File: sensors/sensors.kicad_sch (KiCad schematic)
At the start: 3 parts, among them J1 GPIO, J2 PWM, J3 Conn_01x16

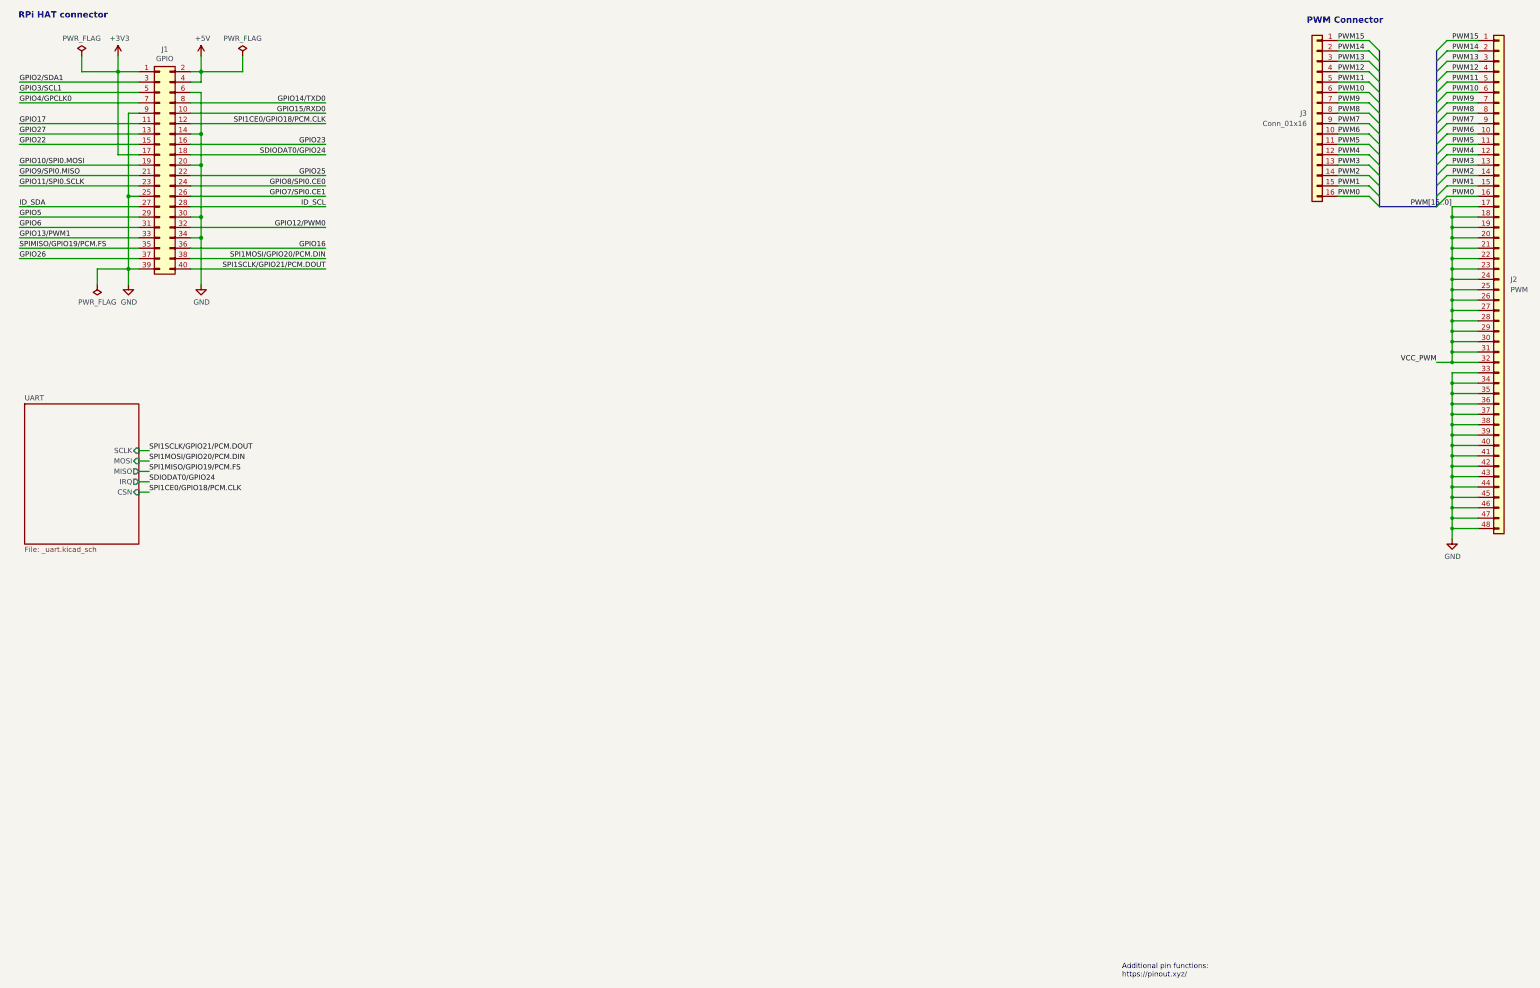
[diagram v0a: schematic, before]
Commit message: add IMU
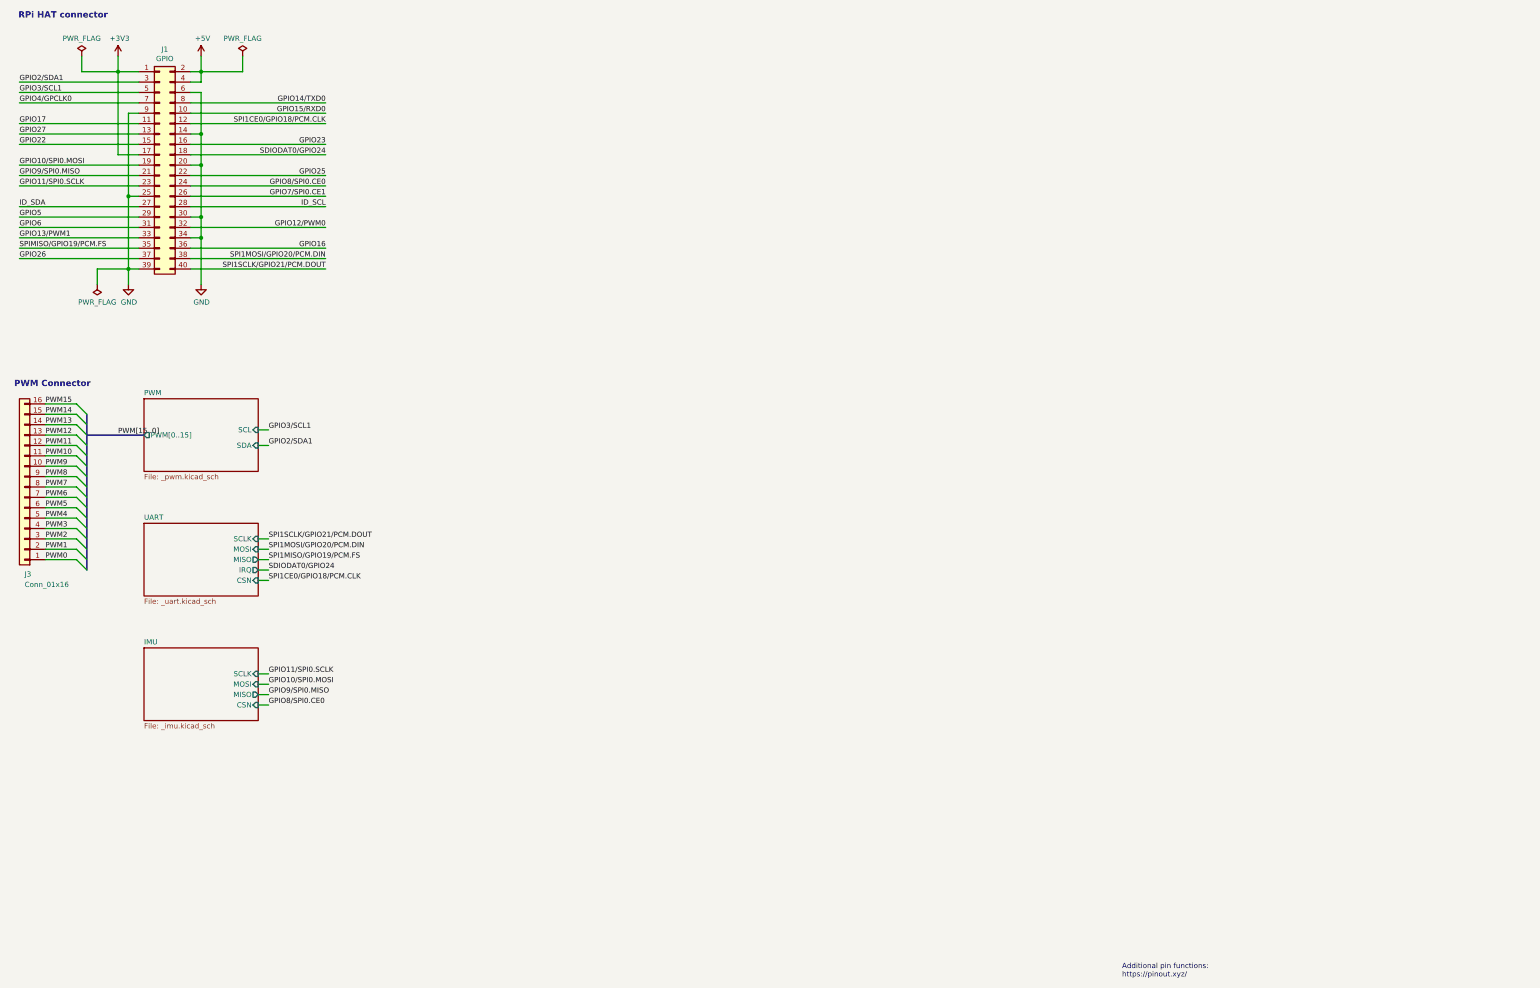
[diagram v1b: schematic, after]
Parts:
- removed J2: PWM, pilotpi:PinHeader_3x16_P2.54mm_Horizontal, symbol Connector_Generic:Conn_01x48
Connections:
- net PWM0: now also J3.1 (Pin_1); no longer J3.16 (Pin_16)
- net PWM1: now also J3.2 (Pin_2); no longer J3.15 (Pin_15)
- net PWM10: now also J3.11 (Pin_11); no longer J3.6 (Pin_6)
- net PWM11: now also J3.12 (Pin_12); no longer J3.5 (Pin_5)
- net PWM12: now also J3.13 (Pin_13); no longer J3.4 (Pin_4)
- net PWM13: now also J3.14 (Pin_14); no longer J3.3 (Pin_3)
- net PWM14: now also J3.15 (Pin_15); no longer J3.2 (Pin_2)
- net PWM15: now also J3.16 (Pin_16); no longer J3.1 (Pin_1)
- net PWM2: now also J3.3 (Pin_3); no longer J3.14 (Pin_14)
- net PWM3: now also J3.4 (Pin_4); no longer J3.13 (Pin_13)
- net PWM4: now also J3.5 (Pin_5); no longer J3.12 (Pin_12)
- net PWM5: now also J3.6 (Pin_6); no longer J3.11 (Pin_11)
- net PWM6: now also J3.7 (Pin_7); no longer J3.10 (Pin_10)
- net PWM7: now also J3.8 (Pin_8); no longer J3.9 (Pin_9)
- net PWM8: now also J3.9 (Pin_9); no longer J3.8 (Pin_8)
- net PWM9: now also J3.10 (Pin_10); no longer J3.7 (Pin_7)
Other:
- added sheet IMU (_imu.kicad_sch)
- added sheet PWM (_pwm.kicad_sch)
- moved on the sheet: J3

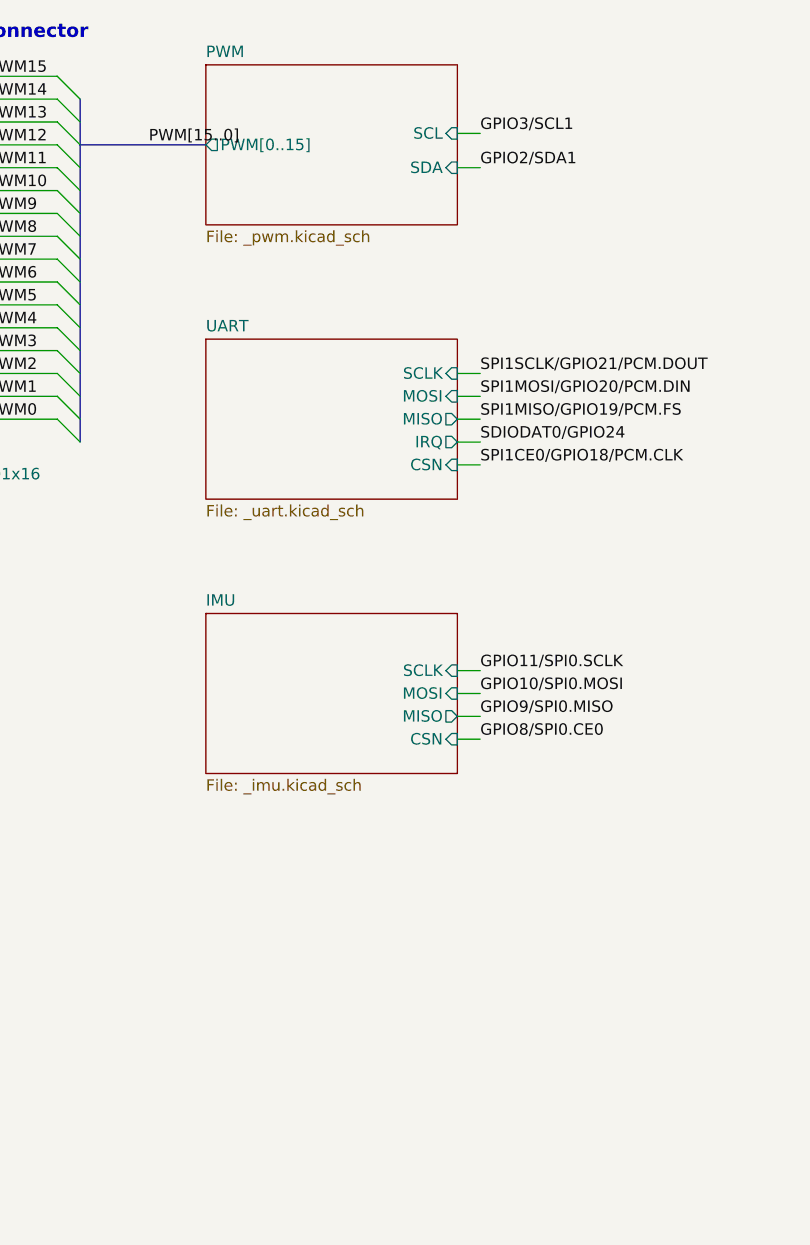
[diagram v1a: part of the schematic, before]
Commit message: add magnetometer
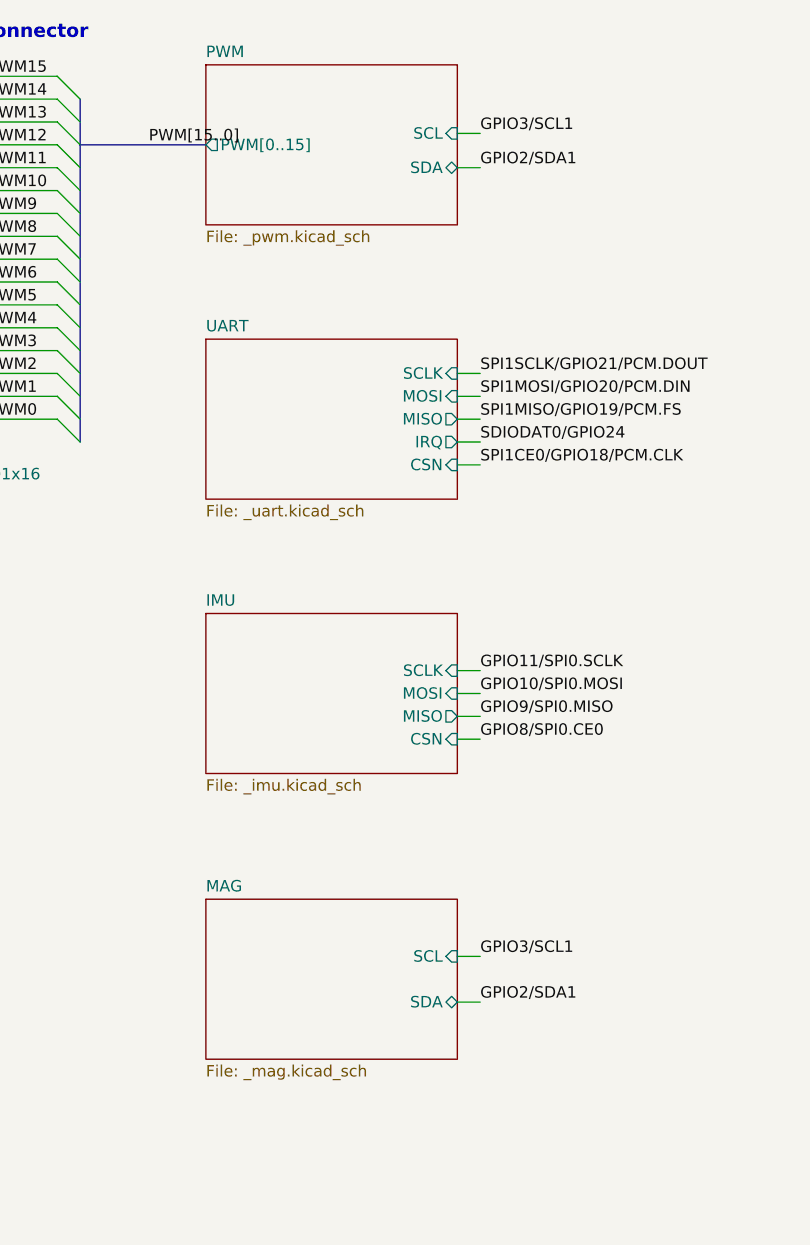
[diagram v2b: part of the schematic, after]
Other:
- added sheet MAG (_mag.kicad_sch)
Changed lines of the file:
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@@
+	(wire
+		(pts
+			(xy 90.17 220.98) (xy 92.71 220.98)
+		)
+		(stroke
+			(width 0)
+			(type default)
+		)
+	)
 	(wire
 		(pts
@@
 			(width 0)
 			(type solid)
+		)
+	)
+	(wire
+		(pts
+			(xy 90.17 215.9) (xy 92.71 215.9)
+		)
+		(stroke
+			(width 0)
+			(type default)
 		)
 	)
@@
 		)
 	)
+	(label "GPIO2{slash}SDA1"
+		(at 92.71 220.98 0)
+		(effects
+			(font
+				(size 1.27 1.27)
+			)
+			(justify left bottom)
+		)
+	)
 	(label "GPIO8{slash}SPI0.CE0"
 		(at 92.71 191.77 0)
@@
 	(label "GPIO27"
 		(at 31.75 52.07 0)
+		(effects
+			(font
+				(size 1.27 1.27)
+			)
+			(justify left bottom)
+		)
+	)
+	(label "GPIO3{slash}SCL1"
+		(at 92.71 215.9 0)
 		(effects
 			(font
@@
 	)
 	(sheet
+		(at 62.23 209.55)
+		(size 27.94 17.78)
+		(exclude_from_sim no)
+		(in_bom yes)
+		(on_board yes)
+		(dnp no)
+		(fields_autoplaced yes)
+		(stroke
+			(width 0.1524)
+			(type solid)
+		)
+		(fill
+			(color 0 0 0 0)
+		)
+		(property "Sheetname" "MAG"
+			(at 62.23 208.8384 0)
+			(show_name no)
+			(do_not_autoplace no)
+			(effects
+				(font
+					(size 1.27 1.27)
+				)
+				(justify left bottom)
+			)
+		)
+		(property "Sheetfile" "_mag.kicad_sch"
+			(at 62.23 227.9146 0)
+			(show_name no)
+			(do_not_autoplace no)
+			(effects
+				(font
+					(size 1.27 1.27)
+				)
+				(justify left top)
+			)
+		)
+		(pin "SCL" input
+			(at 90.17 215.9 0)
+			(effects
+				(font
+					(size 1.27 1.27)
+				)
+				(justify right)
+			)
+		)
+		(pin "SDA" bidirectional
+			(at 90.17 220.98 0)
+			(effects
+				(font
+					(size 1.27 1.27)
+				)
+				(justify right)
+			)
+		)
+		(instances
+			(project "sensors"
+				(path "/e63e39d7-6ac0-4ffd-8aa3-1841a4541b55"
+					(page "5")
+				)
+			)
+		)
+	)
+	(sheet
 		(at 62.23 147.32)
 		(size 27.94 17.78)
@@
 			)
 		)
-		(pin "SDA" input
+		(pin "SDA" bidirectional
 			(at 90.17 128.27 0)
 			(effects

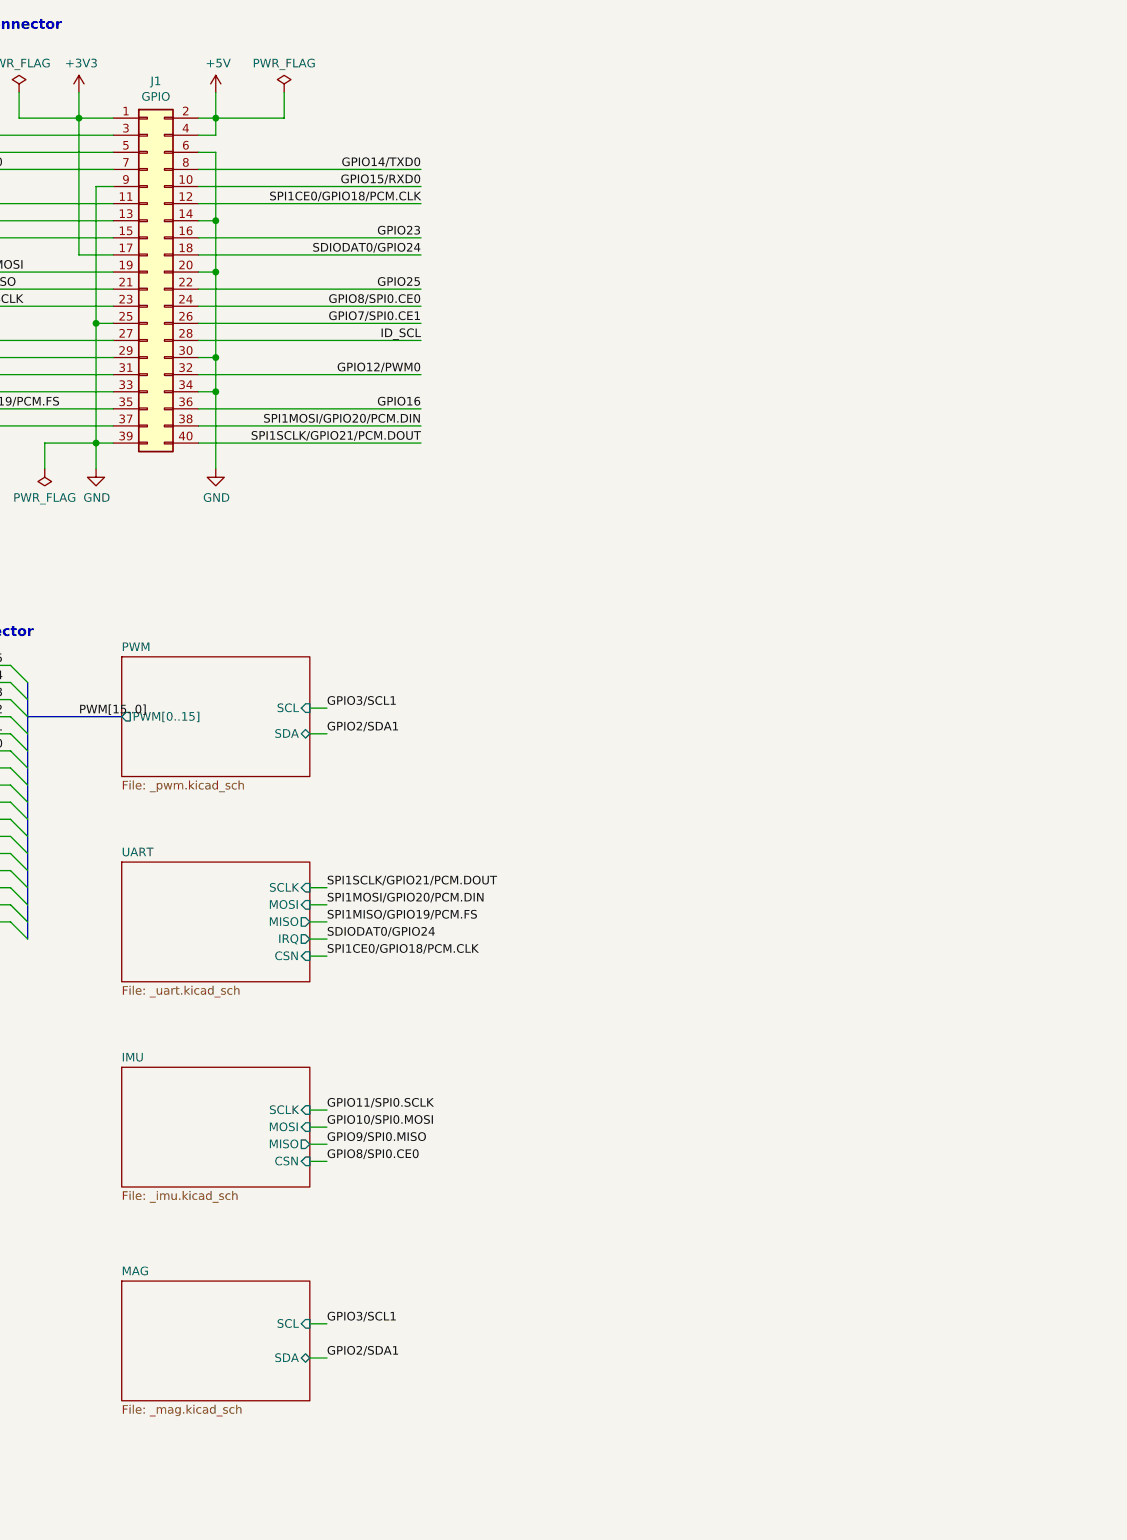
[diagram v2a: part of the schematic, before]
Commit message: add barometer & RC inverter
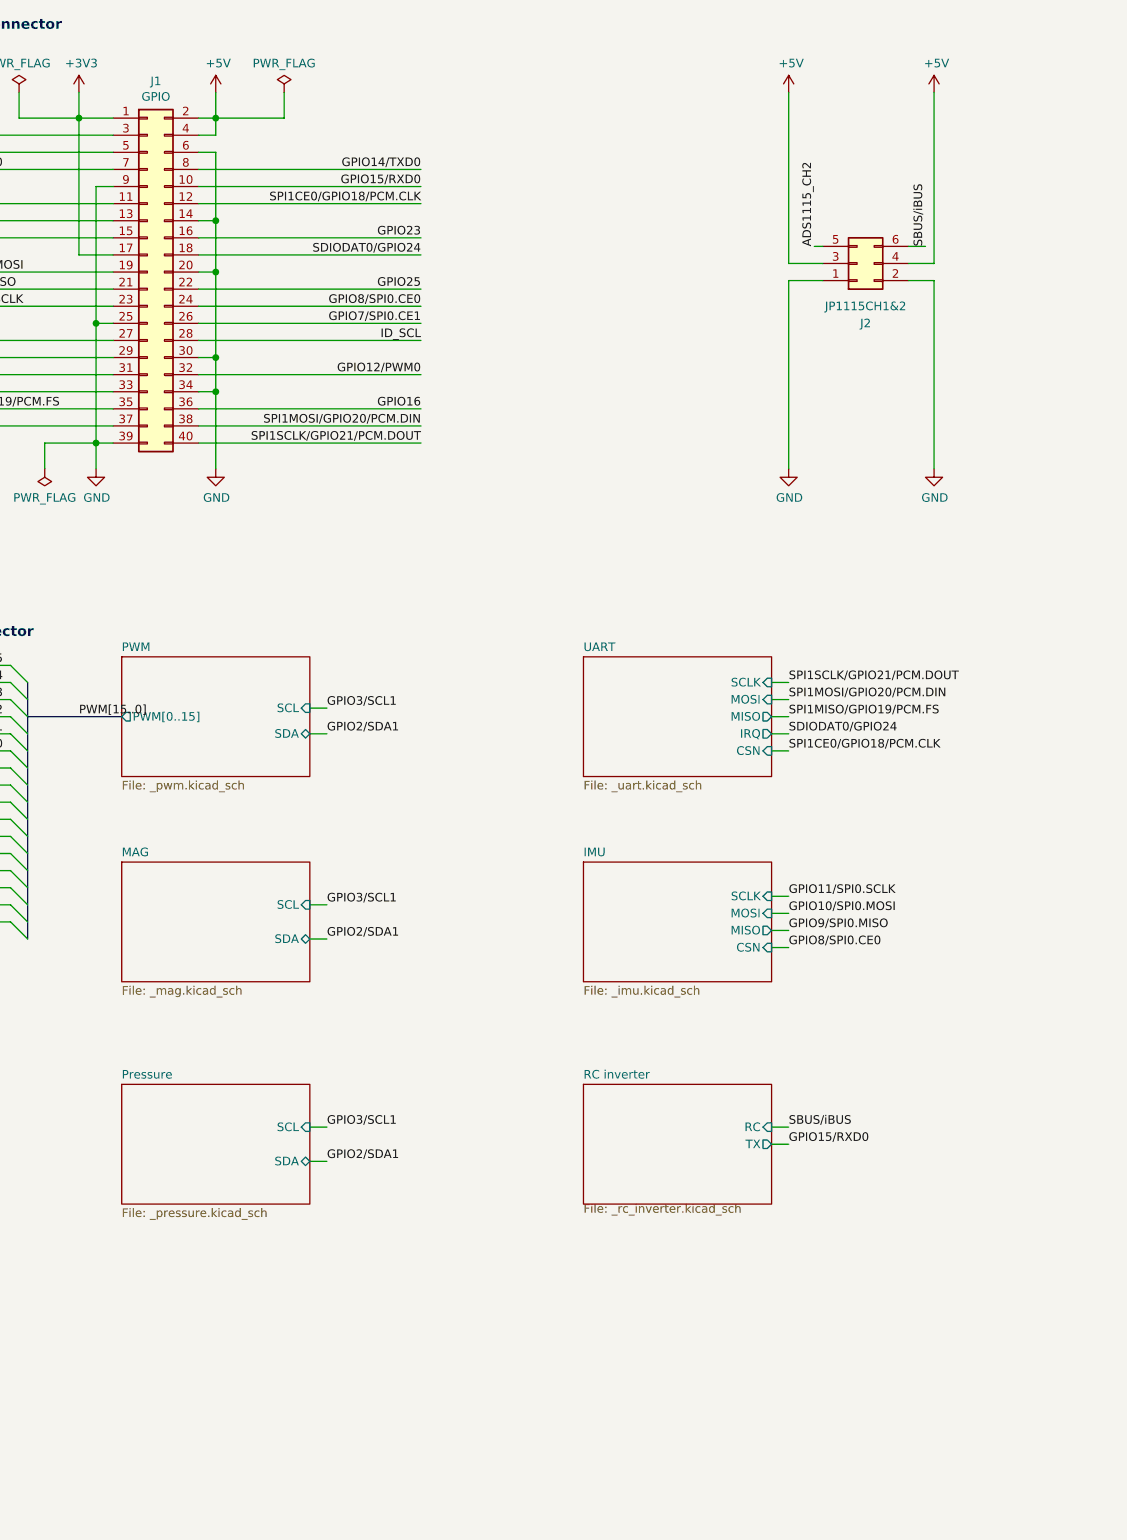
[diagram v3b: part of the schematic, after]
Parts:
- added J2: JP1115CH1&2, Connector_PinHeader_2.54mm:PinHeader_2x03_P2.54mm_Horizontal, symbol Connector_Generic:Conn_02x03_Odd_Even
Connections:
- net +5V: now also J2.3 (Pin_3), J2.4 (Pin_4)
- net GND: now also J2.1 (Pin_1), J2.2 (Pin_2)
- new net ADS1115_CH2: J2.5 (Pin_5)
- new net SBUS/iBUS: J2.6 (Pin_6)
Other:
- added sheet Pressure (_pressure.kicad_sch)
- added sheet RC inverter (_rc_inverter.kicad_sch)
